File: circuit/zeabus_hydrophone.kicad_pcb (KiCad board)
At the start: 4 copper layers, 100 x 70 mm, 157 parts, among them CN1 EPS.00.250.NTN, CN2 EPS.00.250.NTN, CN3 EPS.00.250.NTN, CN4 EPS.00.250.NTN, CON1 ZTEX-V2-FPGA, J1 JTAG, U1 AD9248, U10 MAX5387LAUD+T (10k), U11 MAX5387LAUD+T (10k), U2 AD9248, U3 REF1933, U4 OPA2365, U5 OPA2365, U6 ADA4940-2, U7 OPA2365, U8 OPA2365, U9 ADA4940-2

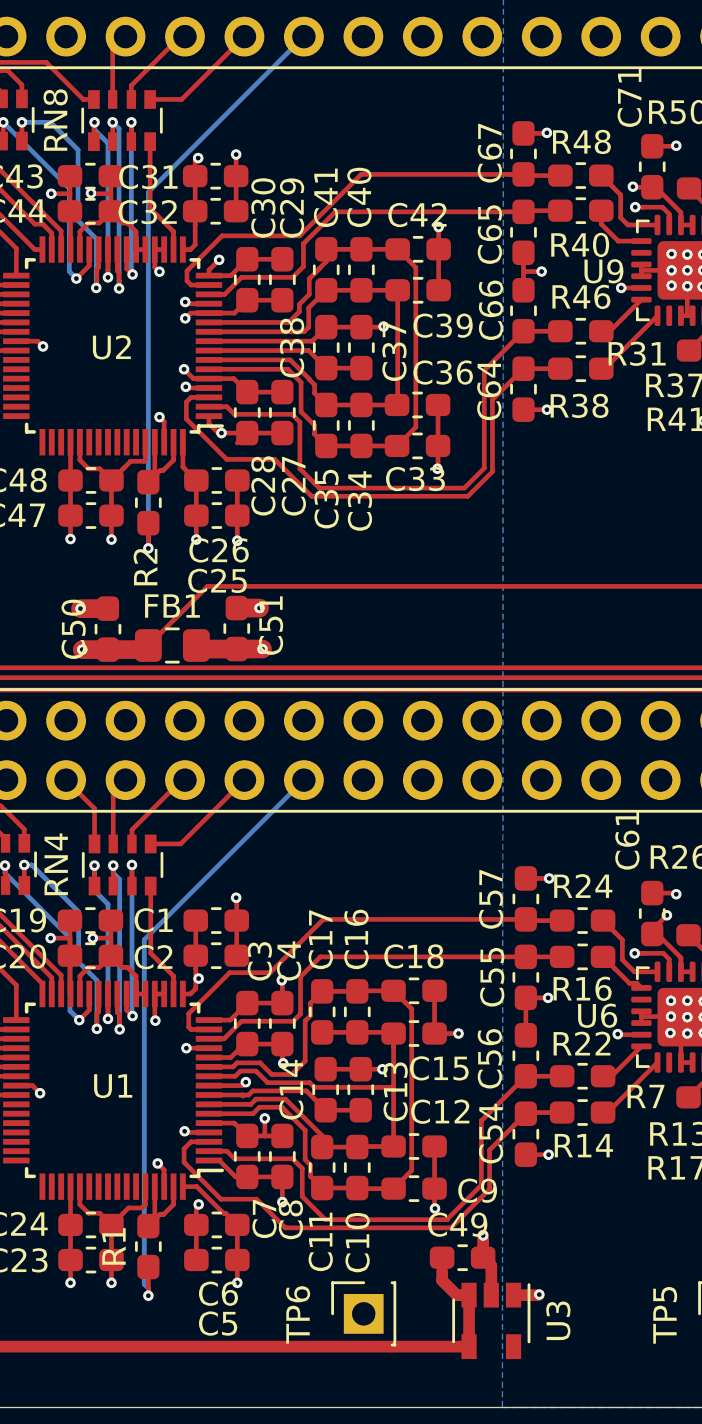
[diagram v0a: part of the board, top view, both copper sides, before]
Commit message: Update C10uF footprint from 0603 to 0805 and add BOM
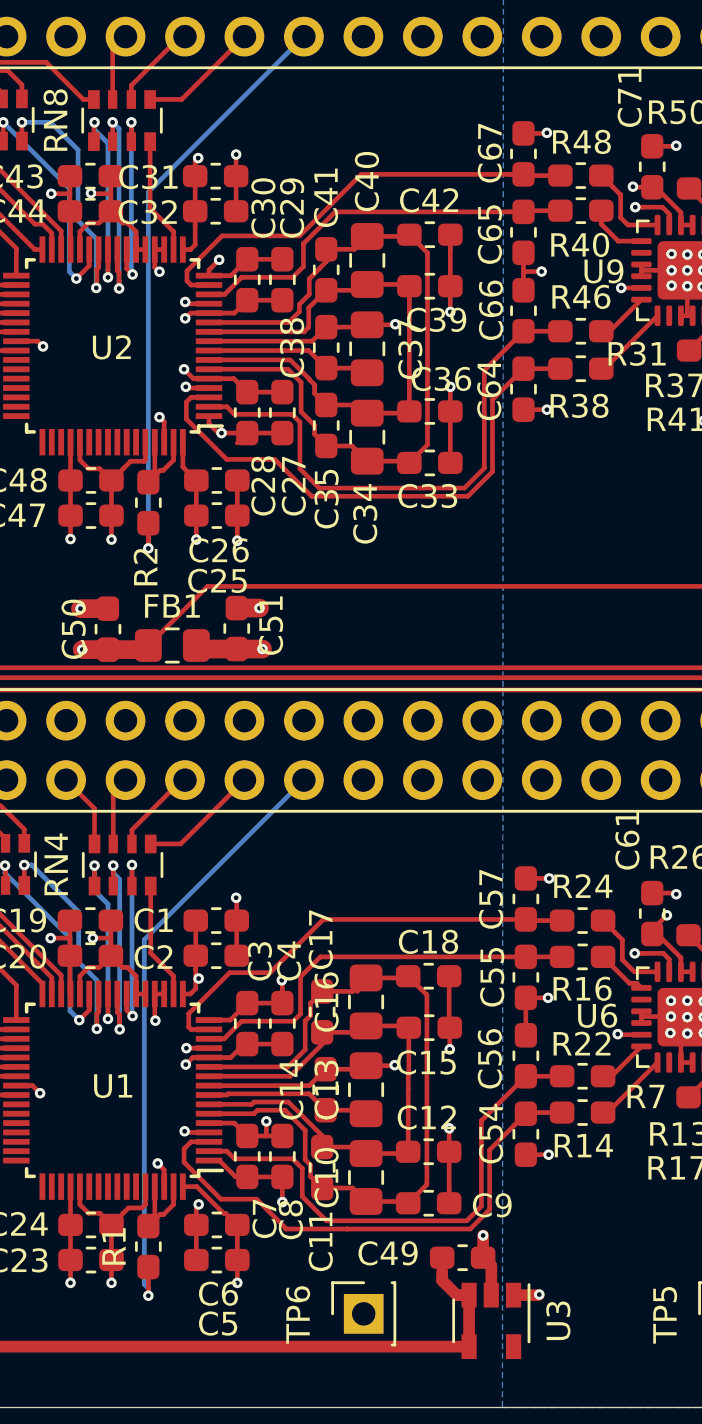
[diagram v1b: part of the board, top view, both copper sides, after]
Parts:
- C10, C13, C16, C34, C37, C40: footprint Capacitor_SMD:C_0603_1608Metric_Pad1.05x0.95mm_HandSolder -> Capacitor_SMD:C_0805_2012Metric_Pad1.15x1.40mm_HandSolder
- C12, C18, C36, C42: value 0.1uf -> 0.1uF
- moved C33 0.90 mm to (139.3, 85.7)
- moved C18 0.88 mm to (139.3, 107.6)
- moved C9 0.88 mm to (139.3, 117.3)
- moved C42 0.80 mm to (139.3, 75.9)
- moved C15 0.70 mm to (139.3, 109.8)
- moved C12 0.66 mm to (139.3, 115.1)
- moved C36 0.59 mm to (139.3, 83.5)
- moved C10 0.57 mm to (136.6, 116.2)
- moved C16 0.57 mm to (136.6, 108.7)
- moved C34 0.56 mm to (136.7, 84.5)
- moved C39 0.53 mm to (139.3, 78.1)
- moved C40 0.47 mm to (136.7, 77.0)
- moved C37 0.25 mm to (136.7, 80.8)
- moved C13 0.22 mm to (136.6, 112.4)
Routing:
- net GNDA: track 153.0 -> 159.7 mm, vias 67 -> 66
- net /REFT2: track 29.6 -> 32.6 mm
- net /REFT1: track 30.5 -> 32.8 mm
- net /REFB2: track 23.2 -> 25.0 mm
- net /analog/VIN1-: track 22.1 -> 22.7 mm
- net /analog/VIN1+: track 21.2 -> 21.7 mm

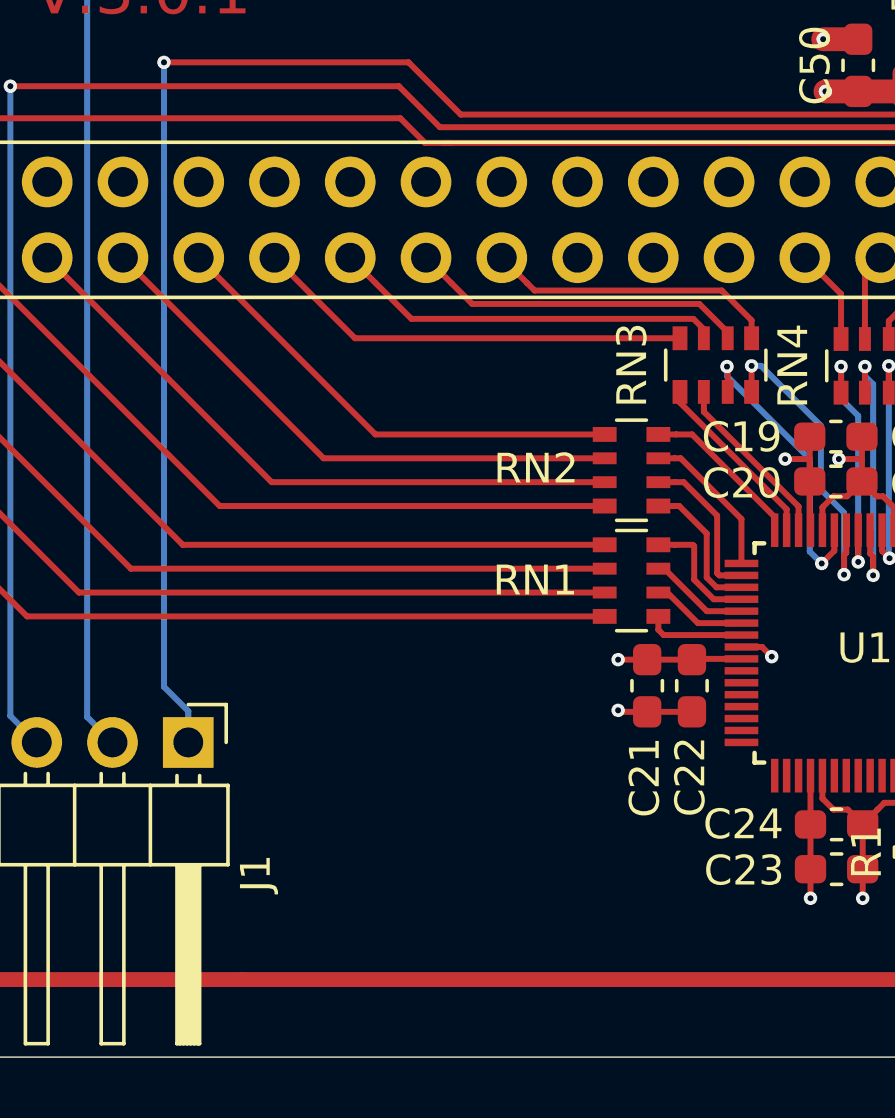
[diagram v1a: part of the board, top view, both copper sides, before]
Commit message: Add green and blue LEDs. Update gerber file.
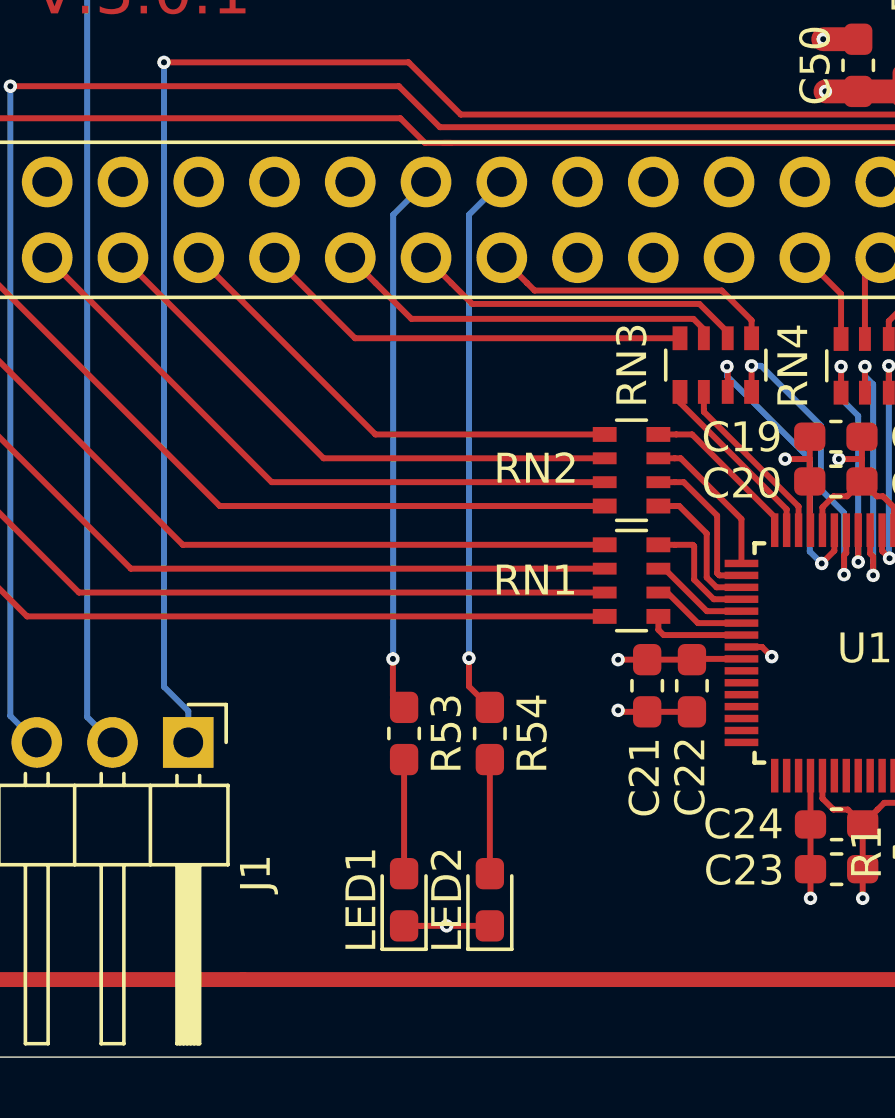
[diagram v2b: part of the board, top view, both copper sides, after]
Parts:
- added LED1: BLUE, LED_SMD:LED_0603_1608Metric_Pad1.05x0.95mm_HandSolder, F.Cu at (110.4, 120.7)
- added LED2: GREEN, LED_SMD:LED_0603_1608Metric_Pad1.05x0.95mm_HandSolder, F.Cu at (113.2, 120.7)
- added R53: 240, Resistor_SMD:R_0603_1608Metric_Pad1.05x0.95mm_HandSolder, F.Cu at (110.4, 115.2)
- added R54: 240, Resistor_SMD:R_0603_1608Metric_Pad1.05x0.95mm_HandSolder, F.Cu at (113.2, 115.2)
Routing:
- net Net-(CON1-PadB14): track 0.00 -> 18.4 mm, vias 0 -> 1
- net Net-(CON1-PadB13): track 0.00 -> 18.2 mm, vias 0 -> 1
- net Net-(LED2-Pad2): track 0.00 -> 3.82 mm
- net Net-(LED1-Pad2): track 0.00 -> 3.82 mm
- net GNDA: track 159.7 -> 162.6 mm, vias 66 -> 67

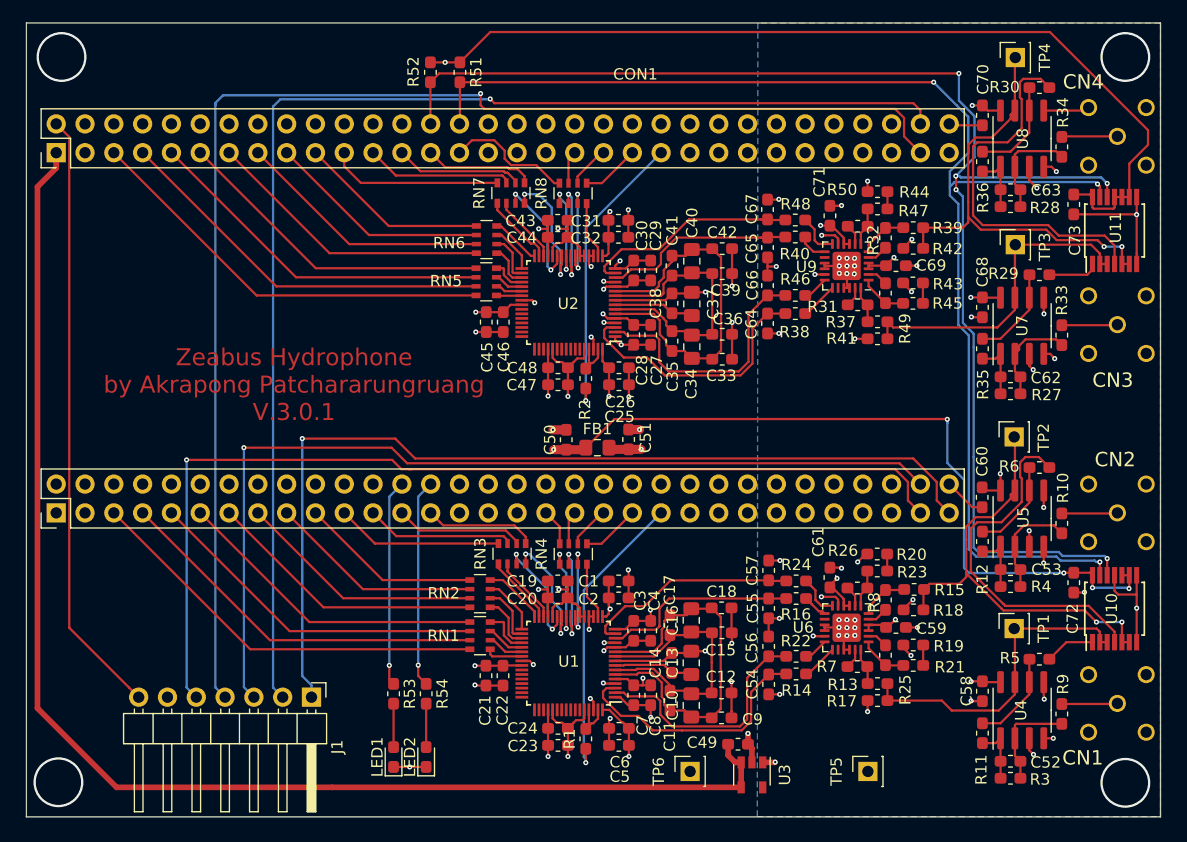
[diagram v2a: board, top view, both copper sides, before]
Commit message: Reorganized PCB layout to minimize difference between ADC data trace lengths. Also finished all elements of FPGA verilog files. The next FPGA coding is the top module.
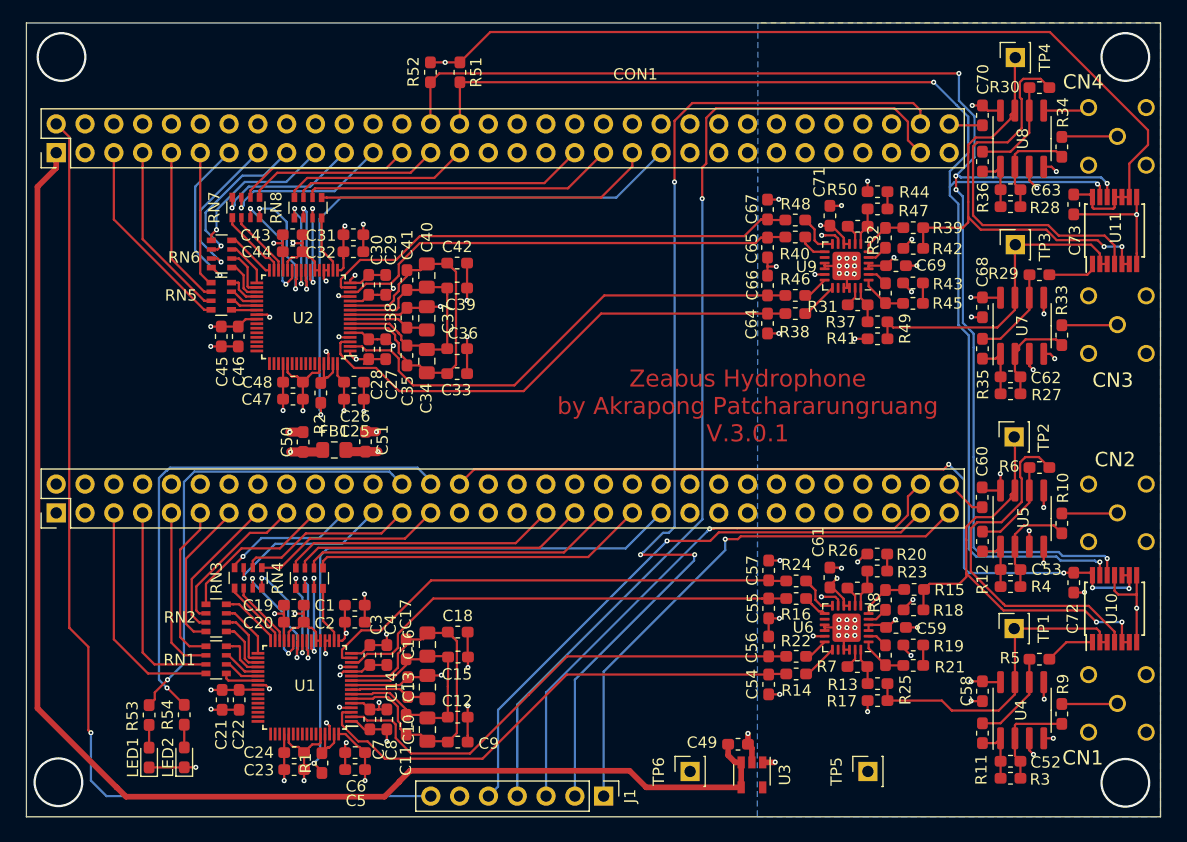
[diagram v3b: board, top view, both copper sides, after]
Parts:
- J1: footprint Connector_PinHeader_2.54mm:PinHeader_1x07_P2.54mm_Horizontal -> Connector_PinHeader_2.54mm:PinHeader_1x07_P2.54mm_Vertical
- moved J1 27.2 mm to (128.9, 124.2)
- moved C27 23.4 mm to (109.7, 84.8)
- moved C28 23.4 mm to (108.2, 84.8)
- moved C29 23.4 mm to (109.7, 79.1)
- moved C30 23.4 mm to (108.2, 79.1)
- moved C34 23.4 mm to (113.3, 85.8)
- moved C35 23.4 mm to (111.6, 85.3)
- moved C37 23.4 mm to (113.3, 82.0)
- moved C38 23.4 mm to (111.6, 82.0)
- moved C40 23.4 mm to (113.3, 78.3)
- moved C41 23.4 mm to (111.6, 78.7)
- moved R2 23.4 mm to (104.0, 88.6)
- moved RN6 23.4 mm to (95.2, 76.4)
- moved RN8 23.4 mm to (102.8, 72.3)
- moved C25 23.4 mm to (106.9, 89.2)
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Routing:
- net Net-(CON1-PadA31): track 89.1 -> 52.4 mm
- net /RESn: track 53.6 -> 89.7 mm, vias 0 -> 1
- net Net-(CON1-PadA32): track 83.8 -> 47.8 mm
- net Net-(CON1-PadB31): track 83.4 -> 50.7 mm
- net Net-(CON1-PadC31): track 119.0 -> 88.5 mm
- net Net-(CON1-PadB14): track 18.4 -> 46.0 mm
- net Net-(CON1-PadC22): track 25.7 -> 50.9 mm
- net Net-(CON1-PadA22): track 26.1 -> 51.3 mm
- net Net-(CON1-PadC21): track 5.14 -> 29.7 mm
- net Net-(CON1-PadA21): track 5.13 -> 29.6 mm
- net Net-(CON1-PadA20): track 3.75 -> 27.9 mm
- net /analog/VIN2+: track 19.1 -> 43.2 mm
- net /analog/VIN2-: track 17.5 -> 41.4 mm
- net /analog/VIN4-: track 17.1 -> 41.0 mm
- net Net-(CON1-PadC20): track 3.75 -> 27.6 mm
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
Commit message: Finish Verilog revision and correct most file errors
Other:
- net class Default removed
- net class VBUS removed
